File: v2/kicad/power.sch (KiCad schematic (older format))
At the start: 14 parts, among them U7 74AC74, U8 74AC14, U9 74AC139

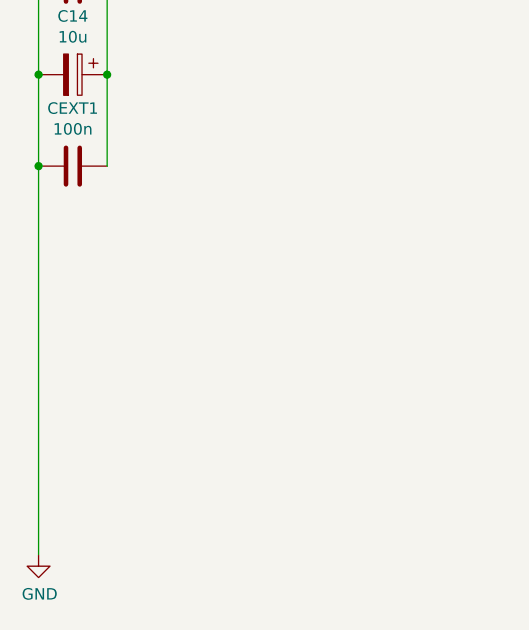
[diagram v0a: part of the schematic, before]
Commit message: All nets verified
All nets have been verified against all design. Even though v2 is not tested yet, at least, the schematic is correct.
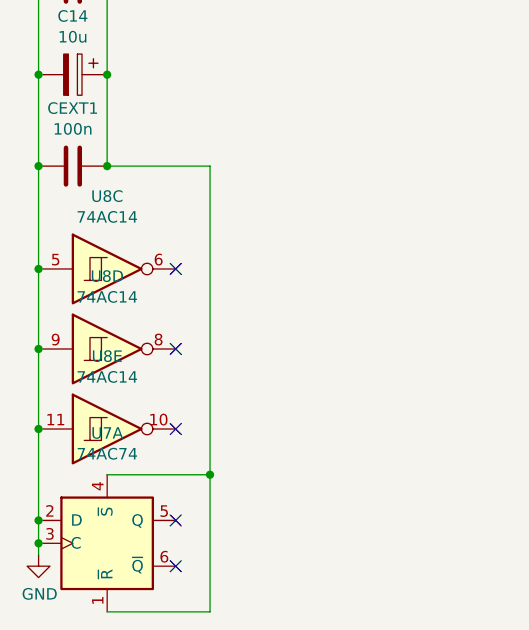
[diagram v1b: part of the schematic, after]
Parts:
- added unit 1 of U7
- added unit 3 of U8
- added unit 4 of U8
- added unit 5 of U8
- U7: footprint Package_SO:SOIC-14_3.9x8.7mm_P1.27mm -> (none)
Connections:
- net GND: now also U7.2 (D), U7.3 (C), U8.11, U8.5, U8.9
- net VCC: now also U7.1 (~R), U7.4 (~S)
- no-connect marks 0 -> 5
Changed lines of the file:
@@
 F 0 "U7" V 5150 1900 50  0000 C CNN
 F 1 "74AC74" V 5150 2300 50  0000 C CNN
-F 2 "Package_SO:SOIC-14_3.9x8.7mm_P1.27mm" H 5400 2150 50  0001 C CNN
+F 2 "" H 5400 2150 50  0001 C CNN
 F 3 "74xx/74hc_hct74.pdf" H 5400 2150 50  0001 C CNN
 	3    5400 2150
@@
 Connection ~ 1900 5400
 Wire Wire Line
-	1900 5400 1900 7100
+	1900 5400 1900 5850
 Wire Wire Line
 	2200 4600 2200 5000
@@
 Wire Wire Line
 	2200 5000 2200 5400
+$Comp
+L 74xx:74LS14 U8
+U 3 1 5FBC2197
+P 2200 5850
+F 0 "U8" H 2200 6167 50  0000 C CNN
+F 1 "74AC14" H 2200 6076 50  0000 C CNN
+F 2 "" H 2200 5850 50  0001 C CNN
+F 3 "http://www.ti.com/lit/gpn/sn74LS14" H 2200 5850 50  0001 C CNN
+	3    2200 5850
+	1    0    0    -1
+$EndComp
+Connection ~ 1900 5850
+Wire Wire Line
+	1900 5850 1900 6200
+$Comp
+L 74xx:74LS14 U8
+U 4 1 5FBC471A
+P 2200 6200
+F 0 "U8" H 2200 6517 50  0000 C CNN
+F 1 "74AC14" H 2200 6426 50  0000 C CNN
+F 2 "" H 2200 6200 50  0001 C CNN
+F 3 "http://www.ti.com/lit/gpn/sn74LS14" H 2200 6200 50  0001 C CNN
+	4    2200 6200
+	1    0    0    -1
+$EndComp
+Connection ~ 1900 6200
+Wire Wire Line
+	1900 6200 1900 6550
+$Comp
+L 74xx:74LS14 U8
+U 5 1 5FBC603E
+P 2200 6550
+F 0 "U8" H 2200 6867 50  0000 C CNN
+F 1 "74AC14" H 2200 6776 50  0000 C CNN
+F 2 "" H 2200 6550 50  0001 C CNN
+F 3 "http://www.ti.com/lit/gpn/sn74LS14" H 2200 6550 50  0001 C CNN
+	5    2200 6550
+	1    0    0    -1
+$EndComp
+Connection ~ 1900 6550
+Wire Wire Line
+	1900 6550 1900 6950
+$Comp
+L 74xx:74HC74 U7
+U 1 1 5FBC9A2E
+P 2200 7050
+F 0 "U7" H 2200 7531 50  0000 C CNN
+F 1 "74AC74" H 2200 7440 50  0000 C CNN
+F 2 "" H 2200 7050 50  0001 C CNN
+F 3 "74xx/74hc_hct74.pdf" H 2200 7050 50  0001 C CNN
+	1    2200 7050
+	1    0    0    -1
+$EndComp
+Wire Wire Line
+	1900 7050 1900 7100
+Wire Wire Line
+	1900 6950 1900 7050
+Connection ~ 1900 6950
+Connection ~ 1900 7050
+Wire Wire Line
+	2200 6750 2650 6750
+Wire Wire Line
+	2200 7350 2650 7350
+Wire Wire Line
+	2650 7350 2650 6750
+Wire Wire Line
+	2650 6750 2650 5400
+Wire Wire Line
+	2650 5400 2200 5400
+Connection ~ 2650 6750
+Connection ~ 2200 5400
+NoConn ~ 2500 5850
+NoConn ~ 2500 6200
+NoConn ~ 2500 6550
+NoConn ~ 2500 6950
+NoConn ~ 2500 7150
 $EndSCHEMATC
